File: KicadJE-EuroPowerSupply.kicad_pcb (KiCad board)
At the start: 2 copper layers, 100 x 100 mm, 116 parts, among them J1 Conn_01x02_Male, J2 Conn_01x02_Male, J3 Conn_01x02_Male, J4 Conn_01x03_Male, J5 Conn_01x03_Male, J6 Conn_01x03_Male, P1 Doepfer_Power_10pin, P10 Doepfer_Power_10pin, P11 Doepfer_Power_10pin, P12 Doepfer_Power_10pin, P2 Doepfer_Power_16pin, P3 Doepfer_Power_10pin, P4 Doepfer_Power_16pin, P5 Doepfer_Power_10pin, P6 Doepfer_Power_16pin, P7 Doepfer_Power_10pin, P8 Doepfer_Power_16pin, P9 Doepfer_Power_10pin, Q1 BD139, Q2 BD140, U1 LM7812_TO220, U2 LM7805_TO220, U3 LM7912_TO220, U4 TL071, U5 LM78M05_TO252, U6 LM78M12_TO252, U7 MC79M12_TO252

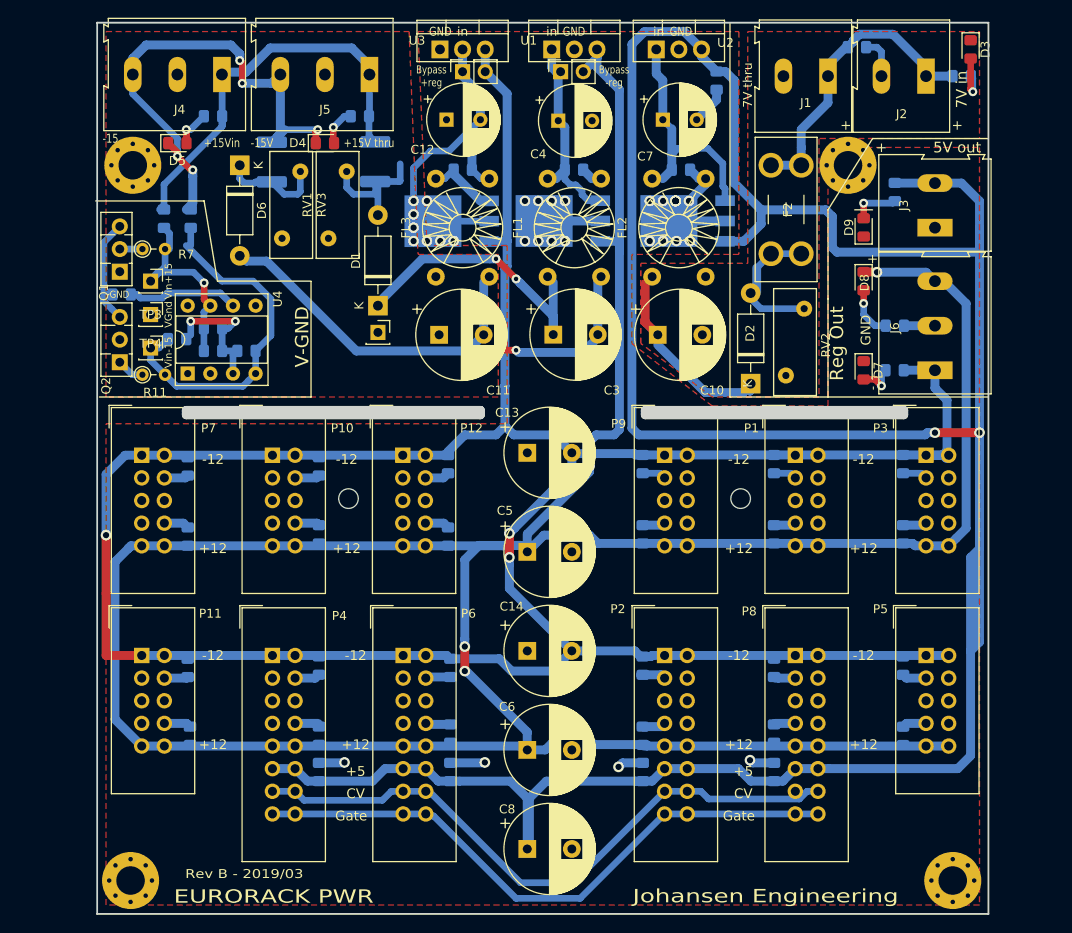
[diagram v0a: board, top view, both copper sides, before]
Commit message: Barel jacks footprints
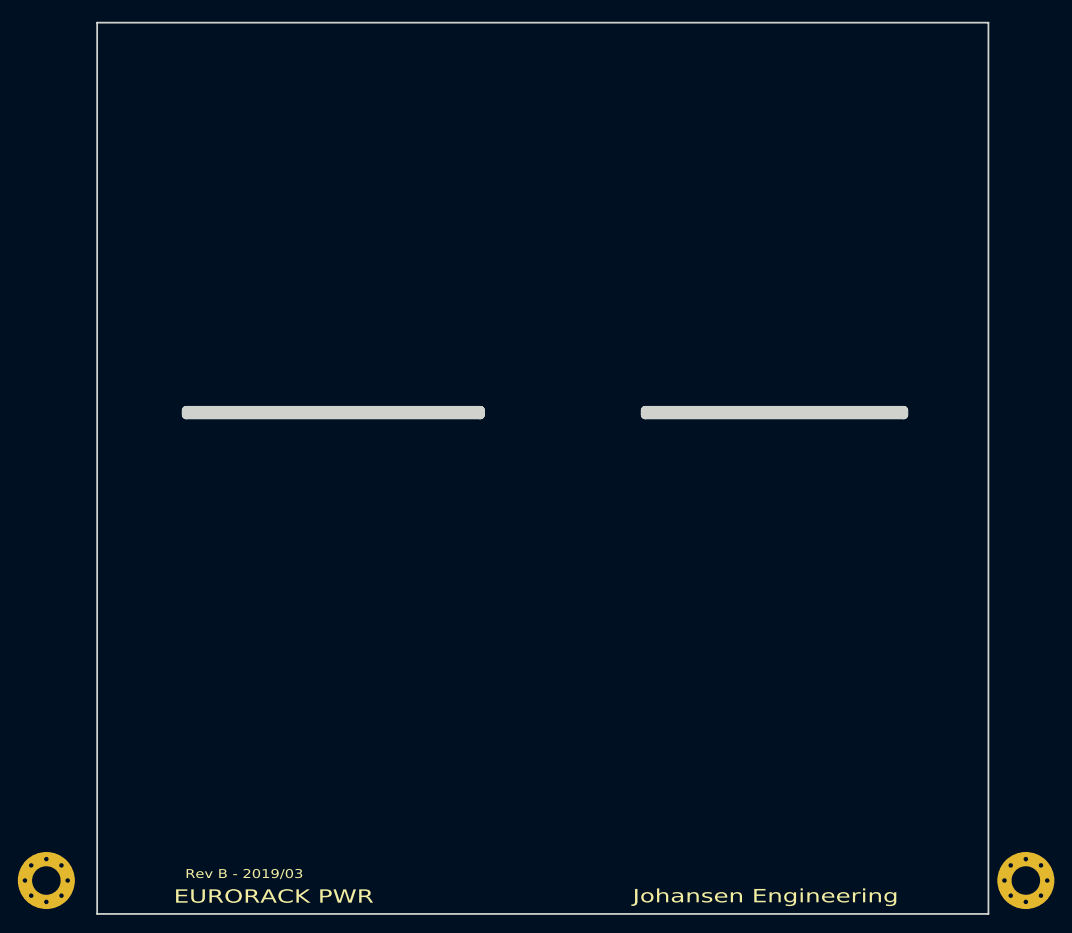
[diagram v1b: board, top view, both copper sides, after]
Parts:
- removed C1, C15, C16, C17, C18, C19, C2, C20, C21, C22, C23, C24, C25, C26, C27, C28, C29, C30, C31, C32, C33, C34, C35, C36, C37, C38, C39, C40, C41, C42, C43, C44, C9: 100n, Capacitor_SMD:C_0805_2012Metric_Pad1.15x1.40mm_HandSolder
- removed C10, C11, C13, C14, C3, C5, C6, C8: 1000uF, Capacitor_THT:CP_Radial_D10.0mm_P5.00mm
- removed C12, C4, C7: 1000uF, Capacitor_THT:CP_Radial_D8.0mm_P3.80mm
- removed C45, C46: 220n, Capacitor_SMD:C_0805_2012Metric_Pad1.15x1.40mm_HandSolder
- removed D1, D2, D6: 1N4001, Diode_THT:D_DO-41_SOD81_P10.16mm_Horizontal
- removed D3, D4, D5, D7, D8, D9: LED, LED_SMD:LED_0805_2012Metric_Pad1.15x1.40mm_HandSolder
- removed F1, F3: Fuse_Small, Fuse:Fuse_1812_4532Metric_Pad1.30x3.40mm_HandSolder
- removed F2: Fuse_Small, Fuse:Fuseholder_Blade_Mini_Keystone_3568
- removed FL1, FL2, FL3: EMI_Filter_CommonMode, Choke_Toroid_ThroughHole:Transformer_Toroid_horizontal_Diameter9mm_Amidon-T30
- removed J1, J2, J3: Conn_01x02_Male, TerminalBlock:TerminalBlock_Altech_AK300-2_P5.00mm
- removed J4, J5, J6: Conn_01x03_Male, TerminalBlock:TerminalBlock_Altech_AK300-3_P5.00mm
- removed JP1, JP2: Jumper_2_Open, Connector_PinSocket_2.54mm:PinSocket_1x02_P2.54mm_Vertical
- removed P1, P10, P11, P12, P3, P5, P7, P9: Doepfer_Power_10pin, Connectors_IDC:IDC-Header_2x05_Pitch2.54mm_Straight
- removed P2, P4, P6, P8: Doepfer_Power_16pin, Connectors_IDC:IDC-Header_2x08_Pitch2.54mm_Straight
- removed Q1: BD139, Package_TO_SOT_THT:TO-126-3_Vertical
- removed Q2: BD140, Package_TO_SOT_THT:TO-126-3_Vertical
- removed R1, R6: 680R, Resistor_SMD:R_0805_2012Metric_Pad1.15x1.40mm_HandSolder
- removed R10, R8, R9: 330r, Resistor_SMD:R_0805_2012Metric_Pad1.15x1.40mm_HandSolder
- removed R11, R7: 10r, Resistor_THT:R_Axial_DIN0204_L3.6mm_D1.6mm_P2.54mm_Vertical
- removed R12, R13: 0R, Resistor_SMD:R_0805_2012Metric_Pad1.15x1.40mm_HandSolder
- removed R2, R3: 3k3, Resistor_SMD:R_0805_2012Metric_Pad1.15x1.40mm_HandSolder
- removed R4, R5: 1k5, Resistor_SMD:R_0805_2012Metric_Pad1.15x1.40mm_HandSolder
- removed the REF** at (128.2, 103.4)
- removed the REF** at (184.2, 66.0)
- removed the REF** at (104.0, 66.0)
- removed the REF** at (172.2, 103.4)
- removed RV1, RV2, RV3: Varistor, Varistor:RV_Disc_D12mm_W4.8mm_P7.5mm
- removed TP1, TP3: VGnd, Connector_PinSocket_2.54mm:PinSocket_1x01_P2.54mm_Vertical
- removed TP2: Vin+15, Connector_PinSocket_2.54mm:PinSocket_1x01_P2.54mm_Vertical
- removed TP4: Vin-15, Connector_PinSocket_2.54mm:PinSocket_1x01_P2.54mm_Vertical
- removed U1: LM7812_TO220, Package_TO_SOT_THT:TO-220-3_Vertical
- removed U2: LM7805_TO220, Package_TO_SOT_THT:TO-220-3_Vertical
- removed U3: LM7912_TO220, Package_TO_SOT_THT:TO-220-3_Vertical
- removed U4: TL071, Package_DIP:DIP-8_W7.62mm_Socket
- removed U5: LM78M05_TO252, Package_TO_SOT_SMD:TO-252-3_TabPin2
- removed U6: LM78M12_TO252, Package_TO_SOT_SMD:TO-252-3_TabPin2
- removed U7: MC79M12_TO252, Package_TO_SOT_SMD:TO-252-3_TabPin2
- moved REF** 9.45 mm to (94.3, 146.2)
- moved REF** 8.20 mm to (204.2, 146.2)
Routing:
- net +12V: track 352.5 -> 0.00 mm, vias 5 -> 0
- net +5V: track 344.2 -> 0.00 mm, vias 2 -> 0
- net -12V: track 304.6 -> 0.00 mm, vias 3 -> 0
- net GND: track 116.9 -> 0.00 mm, vias 24 -> 0
- net CV: track 71.5 -> 0.00 mm
- net Gate: track 69.1 -> 0.00 mm
- net Vin-15: track 61.5 -> 0.00 mm, vias 5 -> 0
- net Vin+15: track 46.6 -> 0.00 mm
- net Net-(C46-Pad2): track 40.4 -> 0.00 mm
- net -15V: track 40.0 -> 0.00 mm, vias 8 -> 0
- net Net-(C11-Pad2): track 39.7 -> 0.00 mm
- net /+5V-ext: track 33.7 -> 0.00 mm
- net Net-(C3-Pad1): track 33.2 -> 0.00 mm, vias 2 -> 0
- net +7.5V: track 27.8 -> 0.00 mm
- net +15V: track 23.2 -> 0.00 mm
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- removed copper zone on F.Cu, net GND
- removed copper zone on F.Cu, net GNDPWR
- removed copper zone on F.Cu, net VinGND
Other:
- board text removed: "+"
- board text removed: "+12"
- board text removed: "+15V thru"
- board text removed: "+15Vin"
- board text removed: "+5"
- board text removed: "-"
- board text removed: "-12"
- board text removed: "-15"
- board text removed: "-15V"
- board text removed: "5V out"
- board text removed: "7V in"
- board text removed: "7V thru"
- board text removed: "Bypass +reg"
- board text removed: "Bypass -reg"
- board text removed: "CV"
- board text removed: "GND"
- board text removed: "Gate"
- board text removed: "Reg Out"
- board text removed: "V-GND"
- board text removed: "in"

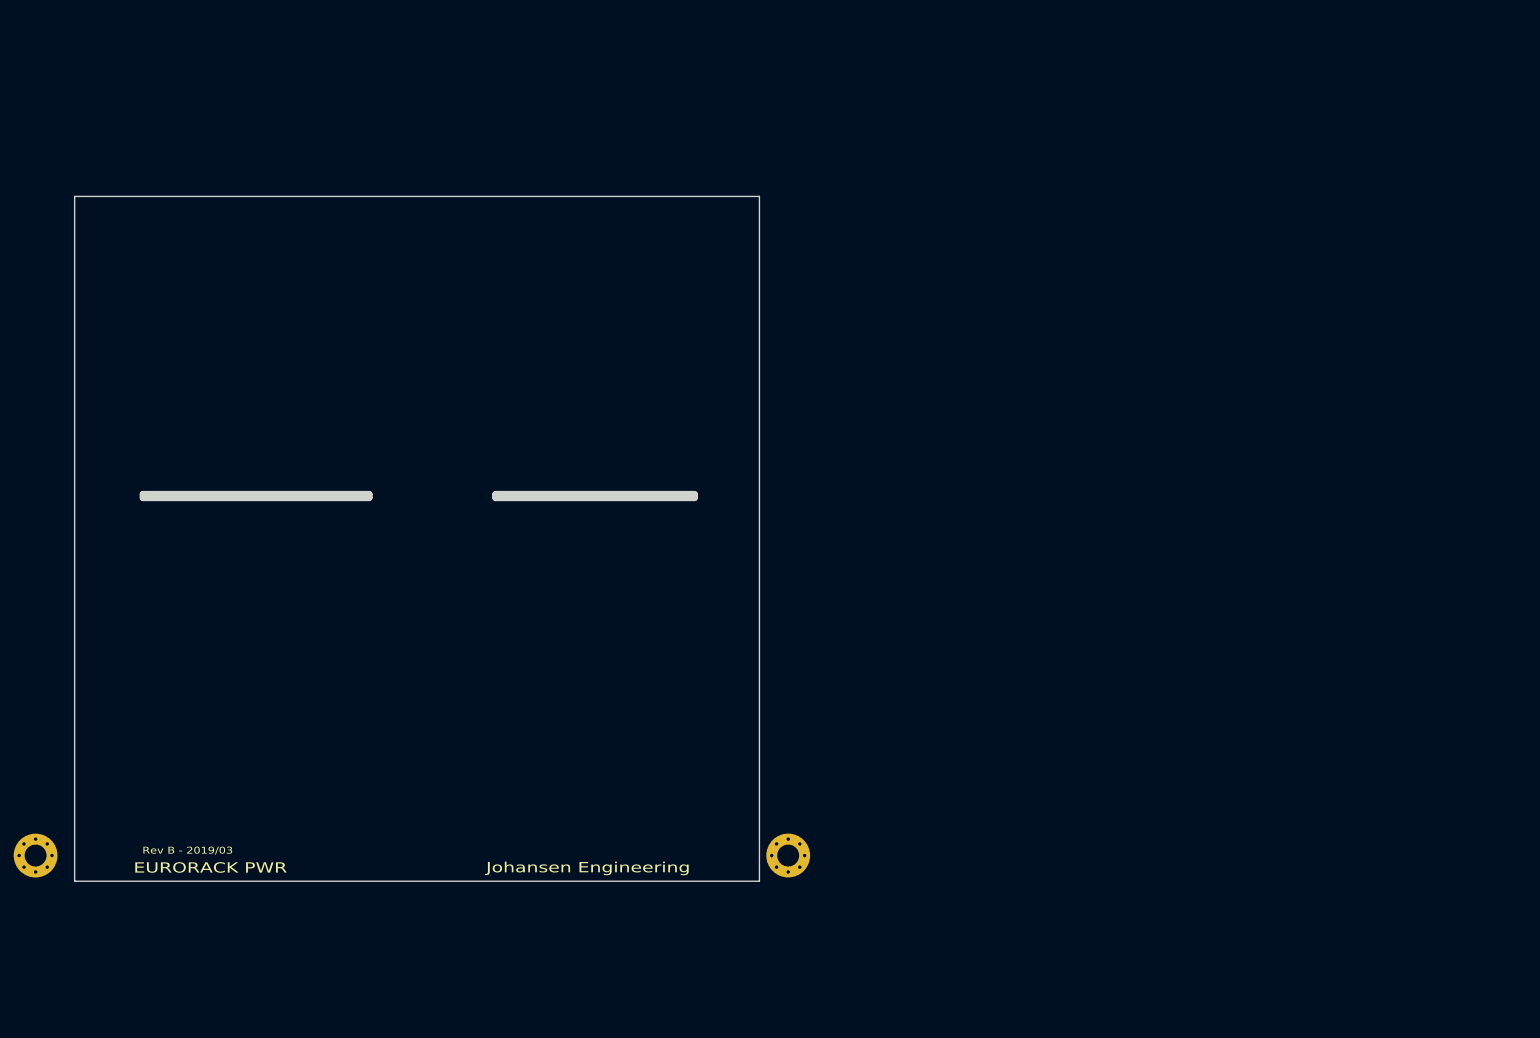
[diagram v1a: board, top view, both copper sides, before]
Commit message: Front Plate and DXF file created - DXF file imported in PCB
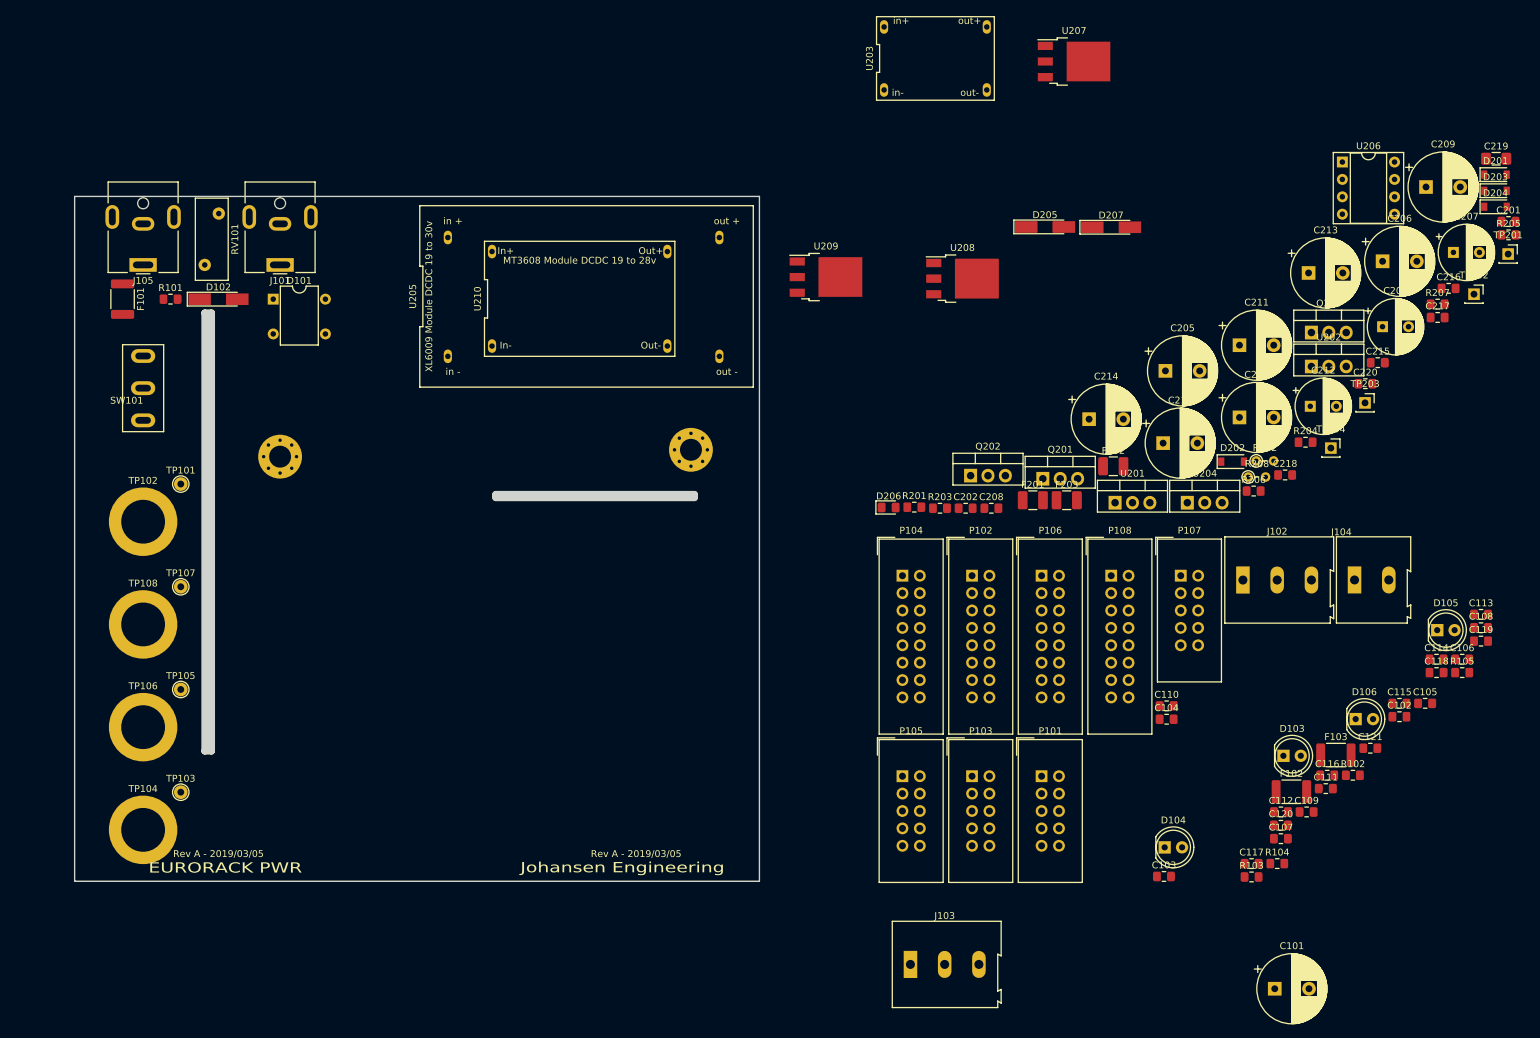
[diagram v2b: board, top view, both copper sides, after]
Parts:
- added C101: 100uF, Capacitor_THT:CP_Radial_D10.0mm_P5.00mm, F.Cu at (275.2, 165.7)
- added C102: 100n, Capacitor_SMD:C_0805_2012Metric_Pad1.15x1.40mm_HandSolder, F.Cu at (293.5, 126.0)
- added C103: 100n, Capacitor_SMD:C_0805_2012Metric_Pad1.15x1.40mm_HandSolder, F.Cu at (259.1, 149.3)
- added C104: 100n, Capacitor_SMD:C_0805_2012Metric_Pad1.15x1.40mm_HandSolder, F.Cu at (259.5, 126.3)
- added C105: 100n, Capacitor_SMD:C_0805_2012Metric_Pad1.15x1.40mm_HandSolder, F.Cu at (297.2, 124.0)
- added C106: 100n, Capacitor_SMD:C_0805_2012Metric_Pad1.15x1.40mm_HandSolder, F.Cu at (302.6, 117.6)
- added C107: 100n, Capacitor_SMD:C_0805_2012Metric_Pad1.15x1.40mm_HandSolder, F.Cu at (276.2, 143.8)
- added C108: 100n, Capacitor_SMD:C_0805_2012Metric_Pad1.15x1.40mm_HandSolder, F.Cu at (305.4, 113.0)
- added C109: 100n, Capacitor_SMD:C_0805_2012Metric_Pad1.15x1.40mm_HandSolder, F.Cu at (279.9, 139.9)
- added C110: 100n, Capacitor_SMD:C_0805_2012Metric_Pad1.15x1.40mm_HandSolder, F.Cu at (259.5, 124.4)
- added C111: 100n, Capacitor_SMD:C_0805_2012Metric_Pad1.15x1.40mm_HandSolder, F.Cu at (282.7, 136.5)
- added C112: 100n, Capacitor_SMD:C_0805_2012Metric_Pad1.15x1.40mm_HandSolder, F.Cu at (276.2, 139.9)
- added C113: 100n, Capacitor_SMD:C_0805_2012Metric_Pad1.15x1.40mm_HandSolder, F.Cu at (305.4, 111.0)
- added C114: 100n, Capacitor_SMD:C_0805_2012Metric_Pad1.15x1.40mm_HandSolder, F.Cu at (298.9, 117.6)
- added C115: 100n, Capacitor_SMD:C_0805_2012Metric_Pad1.15x1.40mm_HandSolder, F.Cu at (293.5, 124.0)
- added C116: 100n, Capacitor_SMD:C_0805_2012Metric_Pad1.15x1.40mm_HandSolder, F.Cu at (282.9, 134.5)
- added C117: 100n, Capacitor_SMD:C_0805_2012Metric_Pad1.15x1.40mm_HandSolder, F.Cu at (271.9, 147.4)
- added C118: 100n, Capacitor_SMD:C_0805_2012Metric_Pad1.15x1.40mm_HandSolder, F.Cu at (298.9, 119.5)
- added C119: 100n, Capacitor_SMD:C_0805_2012Metric_Pad1.15x1.40mm_HandSolder, F.Cu at (305.4, 114.9)
- added C120: 100n, Capacitor_SMD:C_0805_2012Metric_Pad1.15x1.40mm_HandSolder, F.Cu at (276.2, 141.8)
- added C121: 100n, Capacitor_SMD:C_0805_2012Metric_Pad1.15x1.40mm_HandSolder, F.Cu at (289.2, 130.6)
- added C201: 100n, Capacitor_SMD:C_0805_2012Metric_Pad1.15x1.40mm_HandSolder, F.Cu at (309.4, 53.7)
- added C202: 100n, Capacitor_SMD:C_0805_2012Metric_Pad1.15x1.40mm_HandSolder, F.Cu at (230.1, 95.5)
- added C203: 1000uF, Capacitor_THT:CP_Radial_D10.0mm_P5.00mm, F.Cu at (270.1, 82.3)
- added C204: 1000uF, Capacitor_THT:CP_Radial_D8.0mm_P3.80mm, F.Cu at (291.0, 69.0)
- added C205: 1000uF, Capacitor_THT:CP_Radial_D10.0mm_P5.00mm, F.Cu at (259.3, 75.5)
- added C206: 1000uF, Capacitor_THT:CP_Radial_D10.0mm_P5.00mm, F.Cu at (291.0, 59.5)
- added C207: 1000uF, Capacitor_THT:CP_Radial_D8.0mm_P3.80mm, F.Cu at (301.3, 58.2)
- added C208: 100n, Capacitor_SMD:C_0805_2012Metric_Pad1.15x1.40mm_HandSolder, F.Cu at (233.9, 95.5)
- added C209: 1000uF, Capacitor_THT:CP_Radial_D10.0mm_P5.00mm, F.Cu at (297.3, 48.6)
- added C210: 1000uF, Capacitor_THT:CP_Radial_D10.0mm_P5.00mm, F.Cu at (258.9, 86.0)
- added C211: 1000uF, Capacitor_THT:CP_Radial_D10.0mm_P5.00mm, F.Cu at (270.1, 71.7)
- added C212: 1000uF, Capacitor_THT:CP_Radial_D8.0mm_P3.80mm, F.Cu at (280.4, 80.6)
- added C213: 1000uF, Capacitor_THT:CP_Radial_D10.0mm_P5.00mm, F.Cu at (280.2, 61.2)
- added C214: 1000uF, Capacitor_THT:CP_Radial_D10.0mm_P5.00mm, F.Cu at (248.1, 82.5)
- added C215: 100n, Capacitor_SMD:C_0805_2012Metric_Pad1.15x1.40mm_HandSolder, F.Cu at (290.3, 74.3)
- added C216: 220n, Capacitor_SMD:C_0805_2012Metric_Pad1.15x1.40mm_HandSolder, F.Cu at (300.6, 63.4)
- added C217: 220n, Capacitor_SMD:C_0805_2012Metric_Pad1.15x1.40mm_HandSolder, F.Cu at (299.0, 67.7)
- added C218: 220n, Capacitor_SMD:C_0805_2012Metric_Pad1.15x1.40mm_HandSolder, F.Cu at (276.8, 90.7)
- added C219: 1u, Capacitor_SMD:C_1206_3216Metric_Pad1.42x1.75mm_HandSolder, F.Cu at (307.6, 44.5)
- added C220: 220n, Capacitor_SMD:C_0805_2012Metric_Pad1.15x1.40mm_HandSolder, F.Cu at (288.5, 77.3)
- added D101: B125C800DM - DB107, Diode_THT:Diode_Bridge_DIP-4_W7.62mm_P5.08mm, F.Cu at (129.0, 65.0)
- added D102: 27v, Diode_SMD:D_MiniMELF_Handsoldering, F.Cu at (121.0, 65.0)
- added D103: PWR_IN_LED, LED_THT:LED_D5.0mm, F.Cu at (276.5, 131.7)
- added D104: LED, LED_THT:LED_D5.0mm, F.Cu at (259.2, 145.1)
- added D105: LED, LED_THT:LED_D5.0mm, F.Cu at (299.0, 113.3)
- added D106: LED, LED_THT:LED_D5.0mm, F.Cu at (287.1, 126.3)
- added D201: 1N4001, Diode_SMD:D_SOD-123, F.Cu at (307.5, 46.8)
- added D202: 1N4001, Diode_SMD:D_SOD-123, F.Cu at (269.1, 88.7)
- added D203: 1N4001, Diode_SMD:D_SOD-123, F.Cu at (307.5, 49.2)
- added D204: 1N4001, Diode_SMD:D_SOD-123, F.Cu at (307.5, 51.5)
- added D205: 15v, Diode_SMD:D_MiniMELF_Handsoldering, F.Cu at (241.7, 54.5)
- added D206: LED, LED_SMD:LED_0805_2012Metric_Pad1.15x1.40mm_HandSolder, F.Cu at (218.9, 95.4)
- added D207: 15v, Diode_SMD:D_MiniMELF_Handsoldering, F.Cu at (251.3, 54.5)
- added F101: 750mA, Fuse:Fuse_1812_4532Metric_Pad1.30x3.40mm_HandSolder, F.Cu at (107.0, 65.0)
- added F102: 750mA, Fuse:Fuse_1812_4532Metric_Pad1.30x3.40mm_HandSolder, F.Cu at (277.7, 136.9)
- added F103: 750mA, Fuse:Fuse_1812_4532Metric_Pad1.30x3.40mm_HandSolder, F.Cu at (284.2, 131.6)
- added F201: 750mA, Fuse:Fuse_1210_3225Metric_Pad1.42x2.65mm_HandSolder, F.Cu at (239.9, 94.4)
- added F202: 750mA, Fuse:Fuse_1210_3225Metric_Pad1.42x2.65mm_HandSolder, F.Cu at (251.7, 89.4)
- added F203: 750mA, Fuse:Fuse_1210_3225Metric_Pad1.42x2.65mm_HandSolder, F.Cu at (244.9, 94.4)
- added J101: Laptop Power, Connector_BarrelJack:BarrelJack_CUI_PJ-063AH_Horizontal, F.Cu at (130.0, 60.0)
- added J102: +-15V thru, TerminalBlock:TerminalBlock_Altech_AK300-3_P5.00mm, F.Cu at (270.6, 106.0)
- added J103: +-12v out, TerminalBlock:TerminalBlock_Altech_AK300-3_P5.00mm, F.Cu at (222.1, 162.2)
- added J104: +5V out, TerminalBlock:TerminalBlock_Altech_AK300-2_P5.00mm, F.Cu at (286.9, 106.0)
- added J105: Laptop Power Out, Connector_BarrelJack:BarrelJack_CUI_PJ-063AH_Horizontal, F.Cu at (110.0, 60.0)
- added P101: Doepfer_Power_10pin, Connectors_IDC:IDC-Header_2x05_Pitch2.54mm_Straight, F.Cu at (241.2, 134.7)
- added P102: Doepfer_Power_16pin, Connectors_IDC:IDC-Header_2x08_Pitch2.54mm_Straight, F.Cu at (231.0, 105.4)
- added P103: Doepfer_Power_10pin, Connectors_IDC:IDC-Header_2x05_Pitch2.54mm_Straight, F.Cu at (231.0, 134.7)
- added P104: Doepfer_Power_16pin, Connectors_IDC:IDC-Header_2x08_Pitch2.54mm_Straight, F.Cu at (220.9, 105.4)
- added P105: Doepfer_Power_10pin, Connectors_IDC:IDC-Header_2x05_Pitch2.54mm_Straight, F.Cu at (220.9, 134.7)
- added P106: Doepfer_Power_16pin, Connectors_IDC:IDC-Header_2x08_Pitch2.54mm_Straight, F.Cu at (241.2, 105.4)
- added P107: Doepfer_Power_10pin, Connectors_IDC:IDC-Header_2x05_Pitch2.54mm_Straight, F.Cu at (261.5, 105.4)
- added P108: Doepfer_Power_16pin, Connectors_IDC:IDC-Header_2x08_Pitch2.54mm_Straight, F.Cu at (251.4, 105.4)
- added Q201: TIP41, Package_TO_SOT_THT:TO-220-3_Vertical, F.Cu at (241.4, 91.2)
- added Q202: TIP41, Package_TO_SOT_THT:TO-220-3_Vertical, F.Cu at (230.8, 90.8)
- added Q203: TIP42, Package_TO_SOT_THT:TO-220-3_Vertical, F.Cu at (280.6, 69.9)
- added R101: 10r, Resistor_SMD:R_0805_2012Metric_Pad1.15x1.40mm_HandSolder, F.Cu at (114.0, 65.0)
- added R102: 10k, Resistor_SMD:R_0805_2012Metric_Pad1.15x1.40mm_HandSolder, F.Cu at (286.7, 134.5)
- added R103: 4k7, Resistor_SMD:R_0805_2012Metric_Pad1.15x1.40mm_HandSolder, F.Cu at (271.9, 149.4)
- added R104: 1k5, Resistor_SMD:R_0805_2012Metric_Pad1.15x1.40mm_HandSolder, F.Cu at (275.6, 147.4)
- added R105: 4k7, Resistor_SMD:R_0805_2012Metric_Pad1.15x1.40mm_HandSolder, F.Cu at (302.6, 119.5)
- added R201: 0R, Resistor_SMD:R_0805_2012Metric_Pad1.15x1.40mm_HandSolder, F.Cu at (222.6, 95.4)
- added R202: 10r, Resistor_THT:R_Axial_DIN0204_L3.6mm_D1.6mm_P2.54mm_Vertical, F.Cu at (272.5, 88.6)
- added R203: 100r, Resistor_SMD:R_0805_2012Metric_Pad1.15x1.40mm_HandSolder, F.Cu at (226.4, 95.5)
- added R204: 4k70, Resistor_SMD:R_0805_2012Metric_Pad1.15x1.40mm_HandSolder, F.Cu at (279.7, 85.9)
- added R205: 10k, Resistor_SMD:R_0805_2012Metric_Pad1.15x1.40mm_HandSolder, F.Cu at (309.4, 55.6)
- added R206: 330r, Resistor_SMD:R_0805_2012Metric_Pad1.15x1.40mm_HandSolder, F.Cu at (272.2, 93.0)
- added R207: 4k70, Resistor_SMD:R_0805_2012Metric_Pad1.15x1.40mm_HandSolder, F.Cu at (299.0, 65.7)
- added R208: 10r, Resistor_THT:R_Axial_DIN0204_L3.6mm_D1.6mm_P2.54mm_Vertical, F.Cu at (271.4, 91.0)
- added RV101: Varistor, Varistor:RV_Disc_D12mm_W4.8mm_P7.5mm, F.Cu at (119.0, 60.0)
- added SW101: SW_SPDT, AJ-Dropbox-Kicad:SP1MS1, F.Cu at (110.0, 78.0)
- added TP101: RED Sleeve, TestPoint:TestPoint_THTPad_D2.0mm_Drill1.0mm, F.Cu at (115.5, 92.0)
- added TP102: RED Banana, MountingHole:MountingHole_6.4mm_M6_ISO14580_Pad, F.Cu at (110.0, 97.5)
- added TP103: BLUE Sleeve, TestPoint:TestPoint_THTPad_D2.0mm_Drill1.0mm, F.Cu at (115.5, 137.0)
- added TP104: BLUE Banana, MountingHole:MountingHole_6.4mm_M6_ISO14580_Pad, F.Cu at (110.0, 142.5)
- added TP105: BLACK Sleeve, TestPoint:TestPoint_THTPad_D2.0mm_Drill1.0mm, F.Cu at (115.5, 122.0)
- added TP106: BLACK Banana, MountingHole:MountingHole_6.4mm_M6_ISO14580_Pad, F.Cu at (110.0, 127.5)
- added TP107: RED Sleeve, TestPoint:TestPoint_THTPad_D2.0mm_Drill1.0mm, F.Cu at (115.5, 107.0)
- added TP108: RED Banana, MountingHole:MountingHole_6.4mm_M6_ISO14580_Pad, F.Cu at (110.0, 112.5)
- added TP201: VGnd, Connector_PinSocket_2.54mm:PinSocket_1x01_P2.54mm_Vertical, F.Cu at (309.3, 58.4)
- added TP202: Vin+15, Connector_PinSocket_2.54mm:PinSocket_1x01_P2.54mm_Vertical, F.Cu at (304.3, 64.3)
- added TP203: VGnd, Connector_PinSocket_2.54mm:PinSocket_1x01_P2.54mm_Vertical, F.Cu at (288.4, 80.1)
- added TP204: Vin-15, Connector_PinSocket_2.54mm:PinSocket_1x01_P2.54mm_Vertical, F.Cu at (283.4, 86.7)
- added U201: LM7812_TO220, Package_TO_SOT_THT:TO-220-3_Vertical, F.Cu at (251.9, 94.7)
- added U202: LM7805_TO220, Package_TO_SOT_THT:TO-220-3_Vertical, F.Cu at (280.6, 74.8)
- added U203: Step Down Module +15 to 7v - MP2307, AJ:MP2307 DCDC module, F.Cu at (225.7, 29.9)
- added U204: LM7912_TO220, Package_TO_SOT_THT:TO-220-3_Vertical, F.Cu at (262.5, 94.7)
- added U205: XL6009 Module DCDC 19 to 30v, AJ:XL6009-DCDC-Module, F.Cu at (174.8, 64.6)
- added U206: TL071, Package_DIP:DIP-8_W7.62mm_Socket, F.Cu at (285.1, 45.0)
- added U207: LM78M05_TO252, Package_TO_SOT_SMD:TO-252-3_TabPin2, F.Cu at (245.9, 30.3)
- added U208: LM78M12_TO252, Package_TO_SOT_SMD:TO-252-3_TabPin2, F.Cu at (229.7, 62.0)
- added U209: MC79M12_TO252, Package_TO_SOT_SMD:TO-252-3_TabPin2, F.Cu at (209.7, 61.8)
- added U210: MT3608 Module DCDC 19 to 28v, AJ:MT3608 DCDC-Module-USB, F.Cu at (173.8, 65.0)
- moved REF** 68.3 mm to (130.0, 88.0)
- moved REF** 60.9 mm to (190.0, 87.0)
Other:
- outline, holes or cut-outs redrawn
- board text added: "Rev A - 2019/03/05"
- board text removed: "Rev B - 2019/03"
